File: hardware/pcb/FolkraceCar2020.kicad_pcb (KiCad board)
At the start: 2 copper layers, 65 x 68 mm, 73 parts, among them IC1 DRV8874PWPR, J1 Conn_01x02_Male, J2 Raspberry_Pi, J3 Conn_01x02_Male, J4 Conn Servo, J5 Conn Fan, J6 Conn Hall Effect, J7 Conn_01x06_Male, J8 Conn_01x06_Male, J9 Conn_01x06_Male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

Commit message: Finished with rev 1
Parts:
- added R26: R, Resistor_SMD:R_0603_1608Metric, F.Cu at (47.6, 75.4)
- J9: footprint Connector_JST:JST_PH_B6B-PH-K_1x06_P2.00mm_Vertical -> Connector_JST:JST_PH_S6B-PH-K_1x06_P2.00mm_Horizontal
- moved R22 3.35 mm to (68.1, 70.0)
- moved Q2 3.09 mm to (64.7, 71.0)
- moved R11 0.80 mm to (82.4, 84.4)
- moved SW3 0.80 mm to (81.4, 81.6)
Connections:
- net Net-(IC1-Pad3) renamed /NSLEEP
- net Net-(Q1-Pad1) renamed /PGOOD
- net Net-(Q1-Pad3) renamed /~PGOOD
- J2 pad 11: (no net) -> /B2
- J2 pad 12: (no net) -> /~SHDN_TOF_2
- J2 pad 13: (no net) -> /Start
- J2 pad 15: (no net) -> /FAN_CTRL
- J2 pad 16: (no net) -> /~SHDN_TOF_1
- J2 pad 29: (no net) -> /~SHDN_TOF_3
- J2 pad 7: (no net) -> /B1
- J7 pad 4: (no net) -> /~SHDN_TOF_2
- J8 pad 4: (no net) -> /~SHDN_TOF_3
- J9 pad 4: (no net) -> /~SHDN_TOF_1
- MODULE1 pad 3: (no net) -> /Start
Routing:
- net /~SHDN_TOF_1: track 0.00 -> 87.4 mm, vias 0 -> 5
- net /FAN_CTRL: track 2.05 -> 68.9 mm, vias 0 -> 5
- net /Start: track 0.00 -> 60.3 mm, vias 0 -> 2
- net /B1: track 2.84 -> 51.7 mm, vias 0 -> 3
- net /B2: track 2.84 -> 50.9 mm, vias 0 -> 1
- net /PGOOD: track 51.9 -> 98.6 mm, vias 4 -> 8
- net GND: track 23.5 -> 68.9 mm, vias 67 -> 90
- net /~SHDN_TOF_3: track 0.00 -> 12.6 mm, vias 0 -> 2
- net /~SHDN_TOF_2: track 0.00 -> 12.6 mm
- net /NSLEEP: track 5.37 -> 7.00 mm
- net /FAN-: track 2.41 -> 3.64 mm
- net +5V: track 52.2 -> 51.1 mm
- net /SCL: track 145.2 -> 145.7 mm
- net VBUS: track 19.1 -> 19.6 mm
- net /PWM_M: track 84.9 -> 85.4 mm
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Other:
- rule solder_mask_min_width: 0.25 -> 0.1
- board text added: "FAULT"
- board text added: "Odometer"
- board text added: "PWR"
- board text added: "Servo"
- board text added: "TOF 1"
- board text added: "TOF 2"
- board text added: "TOF 3"
- board text added: "laZEr"
- board text added: "laZEr Rev 1 2020-30-30 N. Danielsson"

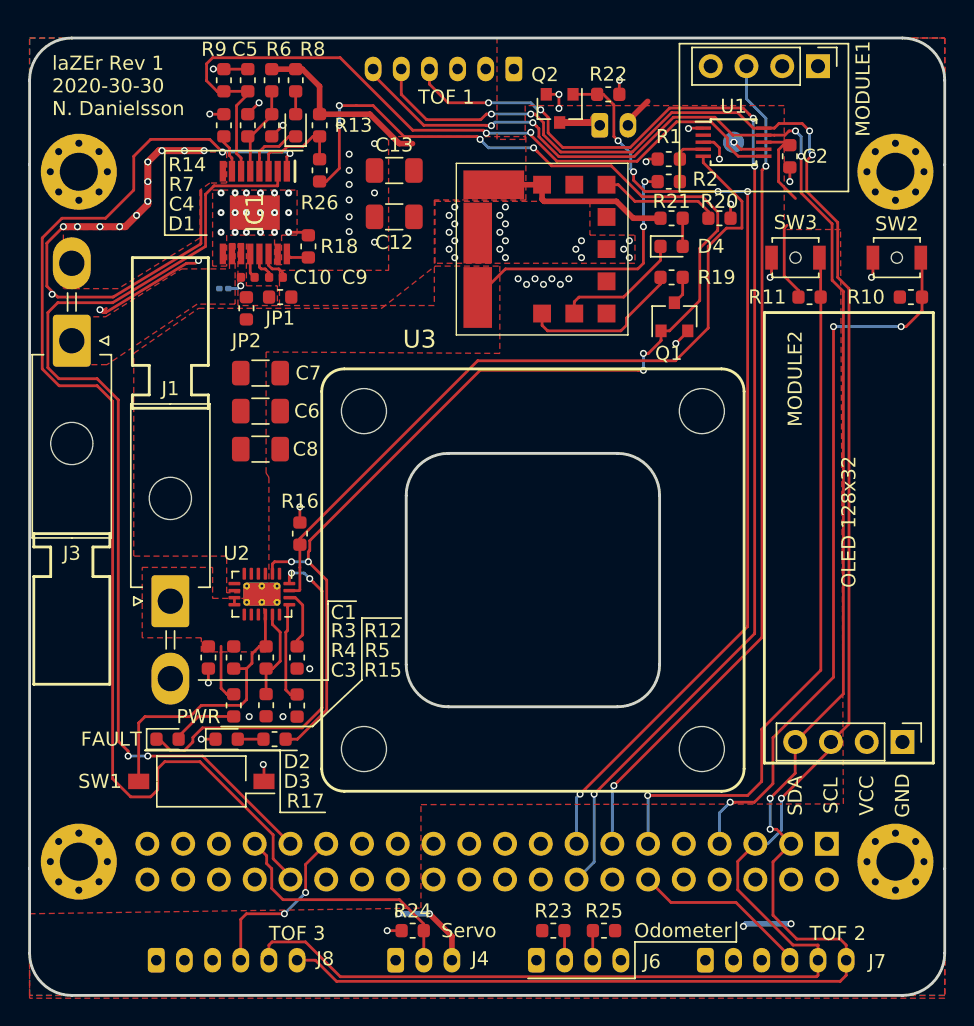
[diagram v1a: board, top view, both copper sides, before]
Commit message: fixed 3v3 error
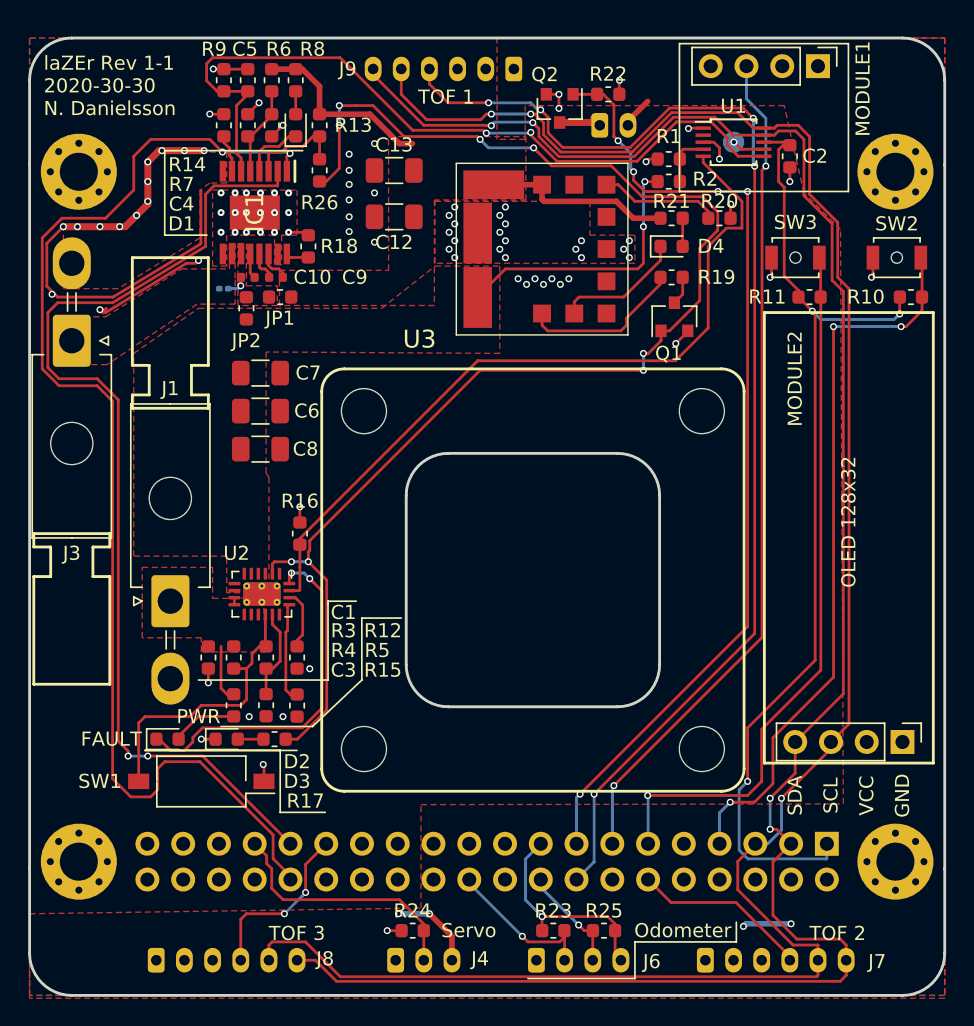
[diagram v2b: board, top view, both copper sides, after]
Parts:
- J9: footprint Connector_JST:JST_PH_S6B-PH-K_1x06_P2.00mm_Horizontal -> Connector_JST:JST_PH_B6B-PH-K_1x06_P2.00mm_Vertical
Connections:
- C2 pad 1: +5V -> +3V3
- J2 pad 1: (no net) -> +3V3
- J2 pad 17: (no net) -> +3V3
- J2 pad 18: (no net) -> /ME_A
- J2 pad 22: (no net) -> /ME_B
- J6 pad 4: +5V -> +3V3
- R10 pad 1: +5V -> +3V3
- R11 pad 1: +5V -> +3V3
- R23 pad 1: +5V -> +3V3
- R25 pad 1: +5V -> +3V3
- U1 pad 8: +5V -> +3V3
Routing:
- net +3V3: track 0.00 -> 86.8 mm, vias 0 -> 4
- net +5V: track 51.1 -> 38.7 mm
- net /ME_B: track 2.11 -> 11.5 mm, vias 0 -> 1
- net /ME_A: track 2.11 -> 7.63 mm, vias 0 -> 1
- net /SCL: track 145.7 -> 145.0 mm, vias 5 -> 3
- net /SDA: vias 6 -> 4
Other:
- board text added: "laZEr Rev 1-1 2020-30-30 N. Danielsson"
- board text removed: "laZEr Rev 1 2020-30-30 N. Danielsson"

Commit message: pcb rev 1-2
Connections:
- MODULE1 pad 1: +5V -> +3V3
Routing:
- net +3V3: track 86.8 -> 93.3 mm, vias 4 -> 5
- net /SCL: track 145.0 -> 145.6 mm
- net /SDA: track 144.4 -> 145.0 mm
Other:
- board text added: "laZEr Rev 1-2 2020-30-30 N. Danielsson"
- board text removed: "laZEr Rev 1-1 2020-30-30 N. Danielsson"
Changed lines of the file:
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@@
     (thickness 1.6)
     (drawings 97)
-    (tracks 723)
+    (tracks 727)
     (zones 0)
     (modules 74)
@@
       (net 1 GND))
     (pad 1 thru_hole rect (at 0 0 270) (size 1.7 1.7) (drill 1) (layers *.Cu *.Mask)
-      (net 2 +5V))
+      (net 53 +3V3))
     (model ${KISYS3DMOD}/Connector_PinHeader_2.54mm.3dshapes/PinHeader_1x04_P2.54mm_Vertical.wrl
       (at (xyz 0 0 0))
@@
     (tags resistor)
     (attr smd)
-    (fp_text reference R6 (at -2.2 -0.5 180) (layer F.SilkS)
+    (fp_text reference R6 (at -2.2 -0.7 180) (layer F.SilkS)
       (effects (font (size 1 1) (thickness 0.15)))
     )
@@
     (tags resistor)
     (attr smd)
-    (fp_text reference R9 (at -2.2 0.7 180) (layer F.SilkS)
+    (fp_text reference R9 (at -2.2 0.5 180) (layer F.SilkS)
       (effects (font (size 1 1) (thickness 0.15)))
     )
@@
     (tags resistor)
     (attr smd)
-    (fp_text reference R8 (at -2.2 -1.2 180) (layer F.SilkS)
+    (fp_text reference R8 (at -2.2 -1.4 180) (layer F.SilkS)
       (effects (font (size 1 1) (thickness 0.15)))
     )
@@
     (tags capacitor)
     (attr smd)
-    (fp_text reference C5 (at -2.2 0.2 180) (layer F.SilkS)
+    (fp_text reference C5 (at -2.2 0 180) (layer F.SilkS)
       (effects (font (size 1 1) (thickness 0.15)))
     )
@@
     (effects (font (size 6 6) (thickness 1) italic) (justify mirror))
   )
-  (gr_text "laZEr Rev 1-1\n2020-30-30\nN. Danielsson" (at 28 69.4) (layer F.SilkS)
+  (gr_text "laZEr Rev 1-2\n2020-30-30\nN. Danielsson" (at 28 69.4) (layer F.SilkS)
     (effects (font (size 1 1) (thickness 0.15)) (justify left))
   )
@@
   (segment (start 57 131.5) (end 57 129.8) (width 0.4) (layer F.Cu) (net 2))
   (via (at 55.4 128.2) (size 0.5) (drill 0.3) (layers F.Cu B.Cu) (net 2))
-  (segment (start 80.7875 73.4) (end 81 73.6125) (width 0.2) (layer F.Cu) (net 53))
-  (segment (start 79.15 73.4) (end 80.7875 73.4) (width 0.2) (layer F.Cu) (net 53))
   (via (at 81.087298 128.912702) (size 0.5) (drill 0.3) (layers F.Cu B.Cu) (net 2))
   (segment (start 77.887298 128.912702) (end 77.7 129.1) (width 0.4) (layer B.Cu) (net 2))
@@
   (segment (start 44.225 130.2) (end 46.6 130.2) (width 0.2) (layer F.Cu) (net 24))
   (segment (start 79.9 72.4) (end 79.15 72.4) (width 0.2) (layer F.Cu) (net 24))
-  (segment (start 81.6 72.2) (end 80.1 72.2) (width 0.2) (layer F.Cu) (net 24))
-  (segment (start 82.4 73) (end 81.6 72.2) (width 0.2) (layer F.Cu) (net 24))
-  (segment (start 82.4 77.1) (end 82.4 73) (width 0.2) (layer F.Cu) (net 24))
+  (segment (start 80.5 71.8) (end 79.9 72.4) (width 0.2) (layer F.Cu) (net 24))
+  (segment (start 82.4 72.6) (end 81.6 71.8) (width 0.2) (layer F.Cu) (net 24))
+  (segment (start 81.6 71.8) (end 80.5 71.8) (width 0.2) (layer F.Cu) (net 24))
+  (segment (start 82.4 77.1) (end 82.4 72.6) (width 0.2) (layer F.Cu) (net 24))
   (segment (start 85.2 114.72) (end 85.2 83.8) (width 0.2) (layer F.Cu) (net 24))
-  (segment (start 84.4 83) (end 84.4 79.1) (width 0.2) (layer F.Cu) (net 24))
   (segment (start 83.92 116) (end 85.2 114.72) (width 0.2) (layer F.Cu) (net 24))
   (segment (start 85.2 83.8) (end 84.4 83) (width 0.2) (layer F.Cu) (net 24))
-  (segment (start 80.1 72.2) (end 79.9 72.4) (width 0.2) (layer F.Cu) (net 24))
+  (segment (start 84.4 83) (end 84.4 79.1) (width 0.2) (layer F.Cu) (net 24))
   (segment (start 84.4 79.1) (end 82.4 77.1) (width 0.2) (layer F.Cu) (net 24))
   (segment (start 81.09 116.29) (end 81.38 116) (width 0.2) (layer F.Cu) (net 25))
@@
   (segment (start 47.3 131.5) (end 48.8 133) (width 0.2) (layer F.Cu) (net 25))
   (segment (start 79.9 72.9) (end 79.15 72.9) (width 0.2) (layer F.Cu) (net 25))
-  (segment (start 80.2 72.6) (end 79.9 72.9) (width 0.2) (layer F.Cu) (net 25))
-  (segment (start 81.4 72.6) (end 80.2 72.6) (width 0.2) (layer F.Cu) (net 25))
-  (segment (start 82 77.2) (end 82 73.2) (width 0.2) (layer F.Cu) (net 25))
+  (segment (start 80.6 72.2) (end 79.9 72.9) (width 0.2) (layer F.Cu) (net 25))
+  (segment (start 81.4 72.2) (end 80.6 72.2) (width 0.2) (layer F.Cu) (net 25))
+  (segment (start 82 72.8) (end 81.4 72.2) (width 0.2) (layer F.Cu) (net 25))
   (segment (start 84.8 112.58) (end 84.8 84) (width 0.2) (layer F.Cu) (net 25))
-  (segment (start 82 73.2) (end 81.4 72.6) (width 0.2) (layer F.Cu) (net 25))
   (segment (start 81.38 116) (end 84.8 112.58) (width 0.2) (layer F.Cu) (net 25))
   (segment (start 84.8 84) (end 84 83.2) (width 0.2) (layer F.Cu) (net 25))
   (segment (start 84 83.2) (end 84 79.2) (width 0.2) (layer F.Cu) (net 25))
+  (segment (start 82 77.2) (end 82 72.8) (width 0.2) (layer F.Cu) (net 25))
   (segment (start 84 79.2) (end 82 77.2) (width 0.2) (layer F.Cu) (net 25))
   (segment (start 55 129.4) (end 55 131.5) (width 0.2) (layer F.Cu) (net 26))
@@
   (segment (start 75.87701 78.359108) (end 74.790892 77.27299) (width 0.2) (layer F.Cu) (net 52))
   (via (at 62.800002 73.8) (size 0.5) (drill 0.3) (layers F.Cu B.Cu) (net 52))
+  (segment (start 80.7875 73.4) (end 81 73.6125) (width 0.2) (layer F.Cu) (net 53))
+  (segment (start 79.15 73.4) (end 80.7875 73.4) (width 0.2) (layer F.Cu) (net 53))
   (via (at 63.4 128.4) (size 0.5) (drill 0.3) (layers F.Cu B.Cu) (net 53))
   (segment (start 62.232999 127.232999) (end 63.4 128.4) (width 0.2) (layer B.Cu) (net 53))
@@
   (segment (start 80.6 76.6) (end 80.6 82.9125) (width 0.2) (layer F.Cu) (net 53))
   (segment (start 80.2 73.9375) (end 80.2 76.2) (width 0.2) (layer F.Cu) (net 53))
+  (via (at 81 72.677) (size 0.5) (drill 0.3) (layers F.Cu B.Cu) (net 53))
+  (segment (start 81 73.6125) (end 81 72.677) (width 0.2) (layer F.Cu) (net 53))
+  (segment (start 83 70.677) (end 83 68) (width 0.2) (layer B.Cu) (net 53))
+  (segment (start 81 72.677) (end 83 70.677) (width 0.2) (layer B.Cu) (net 53))
   (zone (net 3) (net_name +BATT) (layer F.Cu) (hatch edge 0.508)
     (priority 2)
